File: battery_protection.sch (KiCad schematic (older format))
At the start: 5 parts

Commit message: lots of improvements to schematic: fixing decoupling, matching reference designs and recommendations better, connecting pins to esp32 and adding i2c gpio expander
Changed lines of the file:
@@
 EESchema Schematic File Version 4
 LIBS:thingb-eval-hw-cache
-EELAYER 26 0
+EELAYER 29 0
 EELAYER END
 $Descr USLetter 11000 8500
@@
 Wire Wire Line
 	2650 2250 2650 2200
+$Comp
+L power:PWR_FLAG #FLG?
+U 1 1 5D69E1EF
+P 3350 1500
+F 0 "#FLG?" H 3350 1575 50  0001 C CNN
+F 1 "PWR_FLAG" H 3350 1673 50  0000 C CNN
+F 2 "" H 3350 1500 50  0001 C CNN
+F 3 "~" H 3350 1500 50  0001 C CNN
+	1    3350 1500
+	1    0    0    -1
+$EndComp
+Wire Wire Line
+	3350 1500 3350 1550
+Wire Wire Line
+	3350 1550 3100 1550
 $EndSCHEMATC

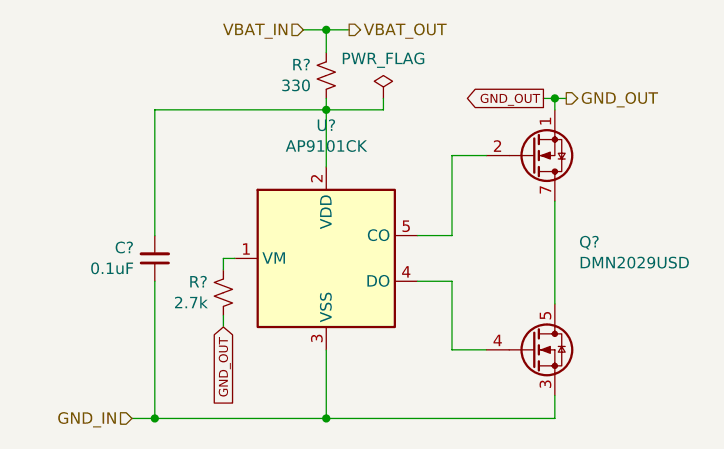
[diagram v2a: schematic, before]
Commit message: change battery protection to dw01 and 8205 pair
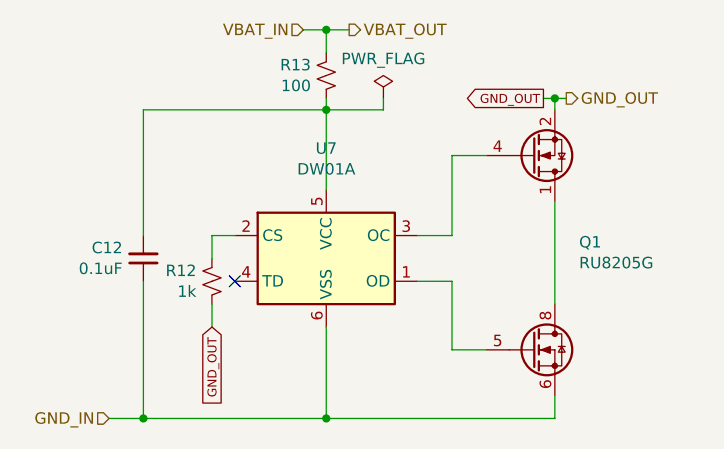
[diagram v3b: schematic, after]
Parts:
- removed Q?: DMN2029USD, Package_SO:SOIC-8_3.9x4.9mm_P1.27mm, symbol thingb:DMN2029USD
- removed U?: AP9101CK, Package_TO_SOT_SMD:SOT-23-5, symbol thingb:AP9101CK
- added Q1: RU8205G, Package_SO:TSSOP-8_4.4x3mm_P0.65mm, symbol thingb:RU8205G
- added U7: DW01A, Package_TO_SOT_SMD:SOT-23-6, symbol thingb:DW01A
- R12: renamed from R?; value 2.7k -> 1k
- R13: renamed from R?; value 330 -> 100
- gave numbers to parts that had none: 1
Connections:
- net GND_IN: now also Q1.6 (S2), Q1.7 (S2), U7.6 (VSS)
- net GND_OUT: now also Q1.2 (S1), Q1.3 (S1)
- net at R12.2: now also U7.2 (CS)
- net at C12.2, R13.1: now also U7.5 (VCC)
- new net: Q1.5 (G2), U7.1 (OD)
- new net: Q1.4 (G1), U7.3 (OC)
- new net: Q1.1 (D1), Q1.8 (D2)
- no-connect marks 0 -> 1
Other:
- moved on the sheet: C12, R12
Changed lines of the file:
@@
 Text HLabel 3000 1200 0    50   Input ~ 0
 VBAT_IN
-Text HLabel 2250 2900 0    50   Input ~ 0
-GND_IN
-$Comp
-L thingb:AP9101CK U?
-U 1 1 5C900992
-P 3100 2200
-F 0 "U?" H 3100 2781 50  0000 C CNN
-F 1 "AP9101CK" H 3100 2690 50  0000 C CNN
-F 2 "Package_TO_SOT_SMD:SOT-23-5" H 3050 2200 50  0001 C CNN
-F 3 "https://www.diodes.com/assets/Datasheets/AP9101C.pdf" H 3100 2250 50  0001 C CNN
-	1    3100 2200
-	1    0    0    -1
-$EndComp
-$Comp
-L thingb:DMN2029USD Q?
-U 1 1 5C90131B
-P 4000 2150
-F 0 "Q?" H 4206 2171 50  0000 L CNN
-F 1 "DMN2029USD" H 4206 2080 50  0000 L CNN
-F 2 "Package_SO:SOIC-8_3.9x4.9mm_P1.27mm" H 4000 2150 50  0001 C CIN
-F 3 "https://www.diodes.com/assets/Datasheets/DMN2029USD.pdf" H 4000 2525 50  0001 L CNN
-	1    4000 2150
-	1    0    0    -1
-$EndComp
 Text HLabel 4150 1500 2    50   Output ~ 0
 GND_OUT
@@
 	3650 2300 3500 2300
 Wire Wire Line
-	4100 2400 4100 1950
-Wire Wire Line
 	4100 2800 4100 2900
 Wire Wire Line
 	4100 2900 3100 2900
 Wire Wire Line
-	3100 2600 3100 2900
+	3100 2500 3100 2900
 Connection ~ 3100 2900
 Wire Wire Line
-	2700 2200 2650 2200
+	2700 2100 2600 2100
 Wire Wire Line
-	2650 2500 2650 2450
+	2600 2500 2600 2400
 $Comp
-L Device:R_Small_US R?
+L Device:R_Small_US R12
 U 1 1 5C90A25D
-P 2650 2350
-F 0 "R?" H 2582 2304 50  0000 R CNN
-F 1 "2.7k" H 2582 2395 50  0000 R CNN
-F 2 "" H 2650 2350 50  0001 C CNN
-F 3 "~" H 2650 2350 50  0001 C CNN
-	1    2650 2350
+P 2600 2300
+F 0 "R12" H 2532 2254 50  0000 R CNN
+F 1 "1k" H 2532 2345 50  0000 R CNN
+F 2 "" H 2600 2300 50  0001 C CNN
+F 3 "~" H 2600 2300 50  0001 C CNN
+	1    2600 2300
 	1    0    0    1
 $EndComp
-Wire Wire Line
-	2250 2900 2350 2900
 Wire Wire Line
 	4100 1550 4100 1500
@@
 	4100 1500 4150 1500
 $Comp
-L Device:C_Small C?
+L Device:C_Small C12
 U 1 1 5C90E66E
-P 2350 2200
-F 0 "C?" H 2259 2154 50  0000 R CNN
-F 1 "0.1uF" H 2259 2245 50  0000 R CNN
-F 2 "" H 2350 2200 50  0001 C CNN
-F 3 "~" H 2350 2200 50  0001 C CNN
-	1    2350 2200
+P 2300 2200
+F 0 "C12" H 2209 2154 50  0000 R CNN
+F 1 "0.1uF" H 2209 2245 50  0000 R CNN
+F 2 "" H 2300 2200 50  0001 C CNN
+F 3 "~" H 2300 2200 50  0001 C CNN
+	1    2300 2200
 	1    0    0    1
 $EndComp
 $Comp
-L Device:R_Small_US R?
+L Device:R_Small_US R13
 U 1 1 5C90E934
 P 3100 1400
-F 0 "R?" H 3033 1354 50  0000 R CNN
-F 1 "330" H 3033 1445 50  0000 R CNN
+F 0 "R13" H 3033 1354 50  0000 R CNN
+F 1 "100" H 3033 1445 50  0000 R CNN
 F 2 "" H 3100 1400 50  0001 C CNN
 F 3 "~" H 3100 1400 50  0001 C CNN
@@
 	3100 1500 3100 1550
 Wire Wire Line
-	3100 1550 2350 1550
+	3100 1550 2300 1550
 Wire Wire Line
-	2350 1550 2350 2100
+	2300 1550 2300 2100
 Connection ~ 3100 1550
 Wire Wire Line
-	3100 1550 3100 1800
+	3100 1550 3100 1900
 Wire Wire Line
-	2350 2300 2350 2900
-Connection ~ 2350 2900
+	2300 2300 2300 2900
+Connection ~ 2300 2900
 Wire Wire Line
-	2350 2900 3100 2900
+	2300 2900 3100 2900
 Text GLabel 4050 1500 0    39   Output ~ 0
 GND_OUT
@@
 	4100 1500 4050 1500
 Connection ~ 4100 1500
-Text GLabel 2650 2500 3    39   Input ~ 0
+Text GLabel 2600 2500 3    39   Input ~ 0
 GND_OUT
 Wire Wire Line
-	2650 2250 2650 2200
+	2600 2200 2600 2100
 $Comp
-L power:PWR_FLAG #FLG?
+L power:PWR_FLAG #FLG02
 U 1 1 5D69E1EF
 P 3350 1500
-F 0 "#FLG?" H 3350 1575 50  0001 C CNN
+F 0 "#FLG02" H 3350 1575 50  0001 C CNN
 F 1 "PWR_FLAG" H 3350 1673 50  0000 C CNN
 F 2 "" H 3350 1500 50  0001 C CNN
@@
 Wire Wire Line
 	3350 1550 3100 1550
+$Comp
+L thingb:DW01A U7
+U 1 1 5D6B96F9
+P 3100 2200
+F 0 "U7" H 3100 2681 50  0000 C CNN
+F 1 "DW01A" H 3100 2590 50  0000 C CNN
+F 2 "Package_TO_SOT_SMD:SOT-23-6" H 3100 2200 50  0001 C CNN
+F 3 "https://datasheet.lcsc.com/szlcsc/1901091236_PUOLOP-DW01A_C351410.pdf" H 3100 2250 50  0001 C CNN
+	1    3100 2200
+	1    0    0    -1
+$EndComp
+Wire Wire Line
+	4100 2400 4100 1950
+$Comp
+L thingb:RU8205G Q1
+U 1 1 5D6BC1E6
+P 4000 2150
+F 0 "Q1" H 4206 2171 50  0000 L CNN
+F 1 "RU8205G" H 4206 2080 50  0000 L CNN
+F 2 "Package_SO:TSSOP-8_4.4x3mm_P0.65mm" H 4000 2150 50  0001 C CIN
+F 3 "https://datasheet.lcsc.com/szlcsc/Shenzhen-ruichips-Semicon-RU8205G_C238491.pdf" H 4000 2550 50  0001 L CNN
+	1    4000 2150
+	1    0    0    -1
+$EndComp
+NoConn ~ 2700 2300
+Wire Wire Line
+	2150 2900 2300 2900
+Text HLabel 2150 2900 0    50   Input ~ 0
+GND_IN
 $EndSCHEMATC

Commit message: reannotate schematic
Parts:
- renumbered Q1 to Q2, R12 to R13, R13 to R14
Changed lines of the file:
@@
 	2600 2500 2600 2400
 $Comp
-L Device:R_Small_US R12
+L Device:R_Small_US R13
 U 1 1 5C90A25D
 P 2600 2300
-F 0 "R12" H 2532 2254 50  0000 R CNN
+F 0 "R13" H 2532 2254 50  0000 R CNN
 F 1 "1k" H 2532 2345 50  0000 R CNN
 F 2 "" H 2600 2300 50  0001 C CNN
@@
 $EndComp
 $Comp
-L Device:R_Small_US R13
+L Device:R_Small_US R14
 U 1 1 5C90E934
 P 3100 1400
-F 0 "R13" H 3033 1354 50  0000 R CNN
+F 0 "R14" H 3033 1354 50  0000 R CNN
 F 1 "100" H 3033 1445 50  0000 R CNN
 F 2 "" H 3100 1400 50  0001 C CNN
@@
 	4100 2400 4100 1950
 $Comp
-L thingb:RU8205G Q1
+L thingb:RU8205G Q2
 U 1 1 5D6BC1E6
 P 4000 2150
-F 0 "Q1" H 4206 2171 50  0000 L CNN
+F 0 "Q2" H 4206 2171 50  0000 L CNN
 F 1 "RU8205G" H 4206 2080 50  0000 L CNN
 F 2 "Package_SO:TSSOP-8_4.4x3mm_P0.65mm" H 4000 2150 50  0001 C CIN

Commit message: associate footprints with all parts
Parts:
- C12: footprint (none) -> Capacitor_SMD:C_0603_1608Metric_Pad1.05x0.95mm_HandSolder
- R13, R14: footprint (none) -> Resistor_SMD:R_0603_1608Metric_Pad1.05x0.95mm_HandSolder
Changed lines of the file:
@@
 F 0 "R13" H 2532 2254 50  0000 R CNN
 F 1 "1k" H 2532 2345 50  0000 R CNN
-F 2 "" H 2600 2300 50  0001 C CNN
+F 2 "Resistor_SMD:R_0603_1608Metric_Pad1.05x0.95mm_HandSolder" H 2600 2300 50  0001 C CNN
 F 3 "~" H 2600 2300 50  0001 C CNN
 	1    2600 2300
@@
 F 0 "C12" H 2209 2154 50  0000 R CNN
 F 1 "0.1uF" H 2209 2245 50  0000 R CNN
-F 2 "" H 2300 2200 50  0001 C CNN
+F 2 "Capacitor_SMD:C_0603_1608Metric_Pad1.05x0.95mm_HandSolder" H 2300 2200 50  0001 C CNN
 F 3 "~" H 2300 2200 50  0001 C CNN
 	1    2300 2200
@@
 F 0 "R14" H 3033 1354 50  0000 R CNN
 F 1 "100" H 3033 1445 50  0000 R CNN
-F 2 "" H 3100 1400 50  0001 C CNN
+F 2 "Resistor_SMD:R_0603_1608Metric_Pad1.05x0.95mm_HandSolder" H 3100 1400 50  0001 C CNN
 F 3 "~" H 3100 1400 50  0001 C CNN
 	1    3100 1400
